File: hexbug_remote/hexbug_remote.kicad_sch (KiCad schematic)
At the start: 34 parts, among them J1 USB C, J2 Conn_01x02, J3 Conn_01x06, SW1 Tactile, SW2 Tactile, SW3 Tactile, SW4 Tactile, SW5 Tactile, SW6 Tactile, SW7 SP4T, SW8 SPDT, U1 BQ21040, U2 RT9078, U3 MSPM0L1304

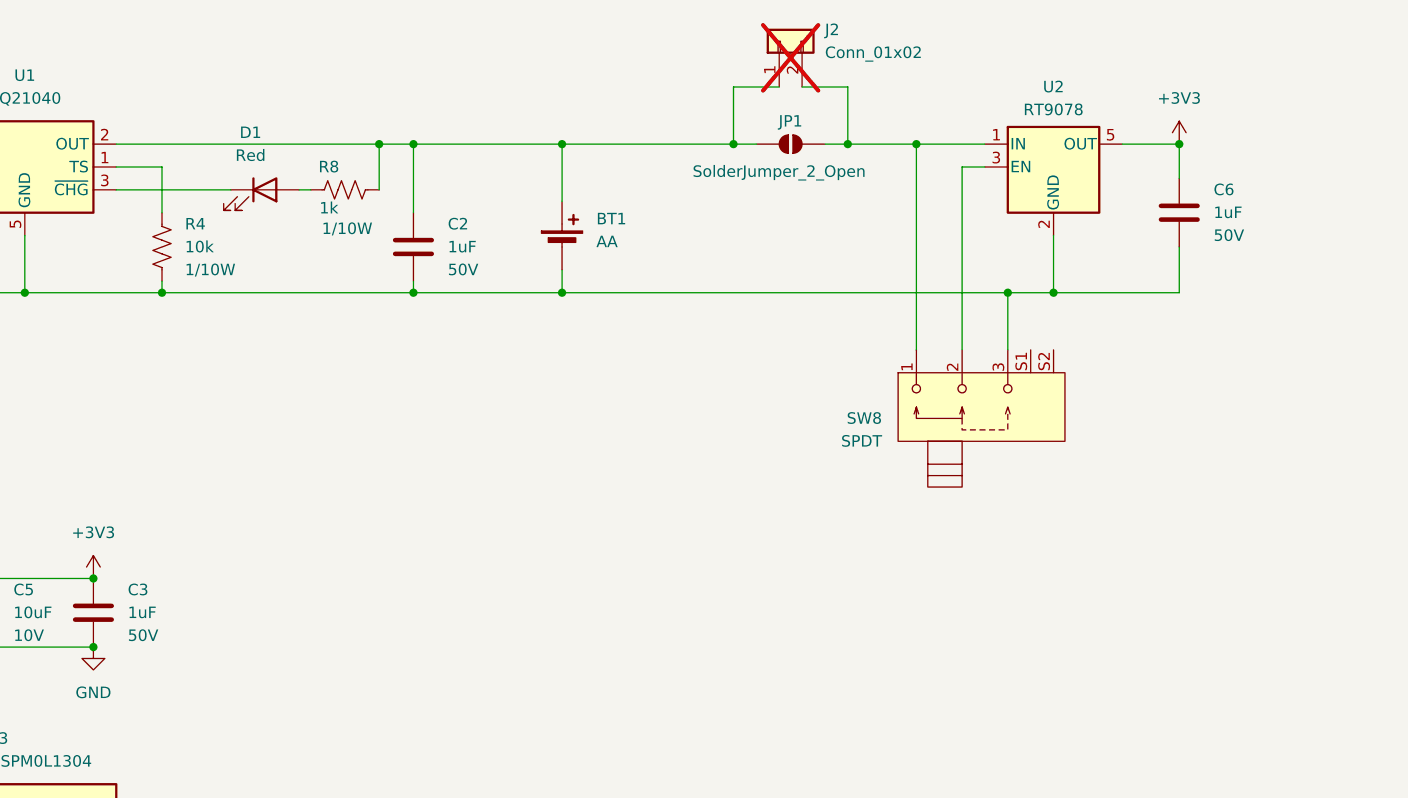
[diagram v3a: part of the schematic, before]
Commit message: Add Battery Protection
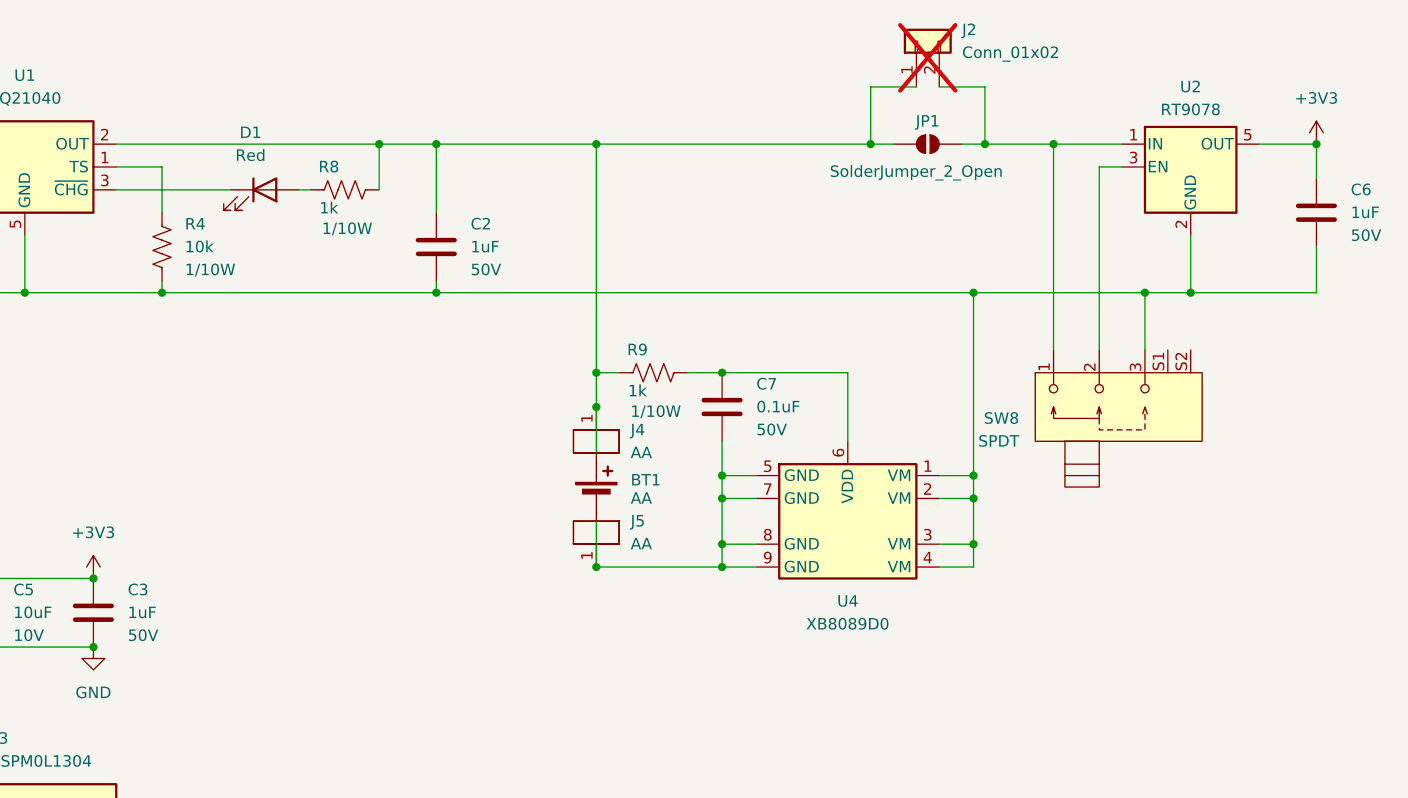
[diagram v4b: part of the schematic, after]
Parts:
- added C7: 0.1uF, Capacitor_SMD:C_0603_1608Metric, symbol -Local_Lib:Capacitors/CAP-000003
- added J4, J5: AA, Local_Footprints:Battery_Clip_Keystone_53, symbol -Local_Lib:Mechanical/MECH-000006
- added R9: 1k, Resistor_SMD:R_0603_1608Metric_Pad0.98x0.95mm_HandSolder, symbol -Local_Lib:Resistors/RES-000005
- added U4: XB8089D0, Local_Footprints:SOP-8-1EP_3.9x4.9mm_P1.27mm_EP2.4x3.3mm, symbol -Local_Lib:Integrated Circuits/IC-000004
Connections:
- net GND: now also U4.1 (VM), U4.2 (VM), U4.3 (VM), U4.4 (VM); no longer BT1.2 (-)
- net at BT1.1 (+), C2.1, J2.1 (Pin_1)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: now also J4.1, R9.2
- new net: BT1.2 (-), C7.2, J5.1, U4.5 (GND), U4.7 (GND), U4.8 (GND), U4.9 (GND)
- new net: C7.1, R9.1, U4.6 (VDD)
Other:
- moved on the sheet: BT1, C2, C6, J2, JP1, SW8, U2

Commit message: Update Step File
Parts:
- BT1: now not fitted
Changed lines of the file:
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@@
 		(in_bom yes)
 		(on_board yes)
-		(dnp no)
+		(dnp yes)
 		(property "Reference" "BT1"
 			(at 179.07 80.518 0)
